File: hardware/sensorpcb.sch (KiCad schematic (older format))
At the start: 7 parts, among them P1 CONN_01X02

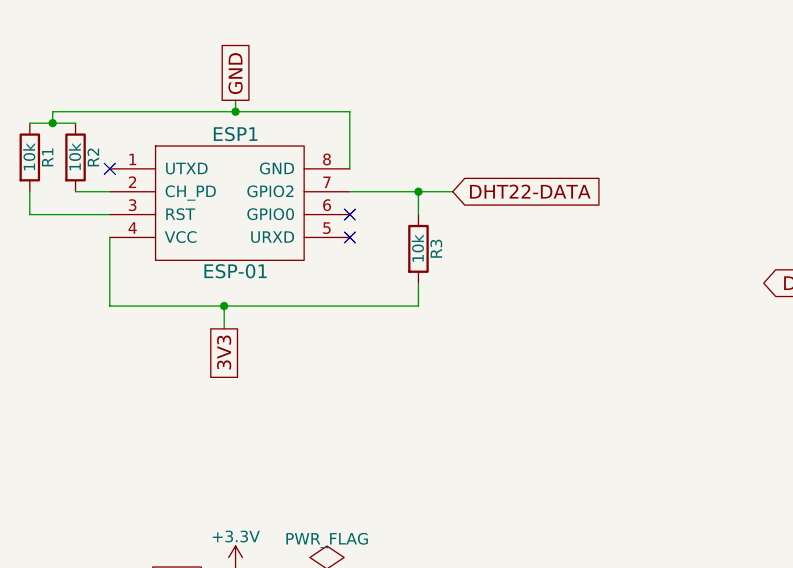
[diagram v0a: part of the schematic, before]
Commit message: corrected schematic: R1 and R2 are pullups, not pulldowns!
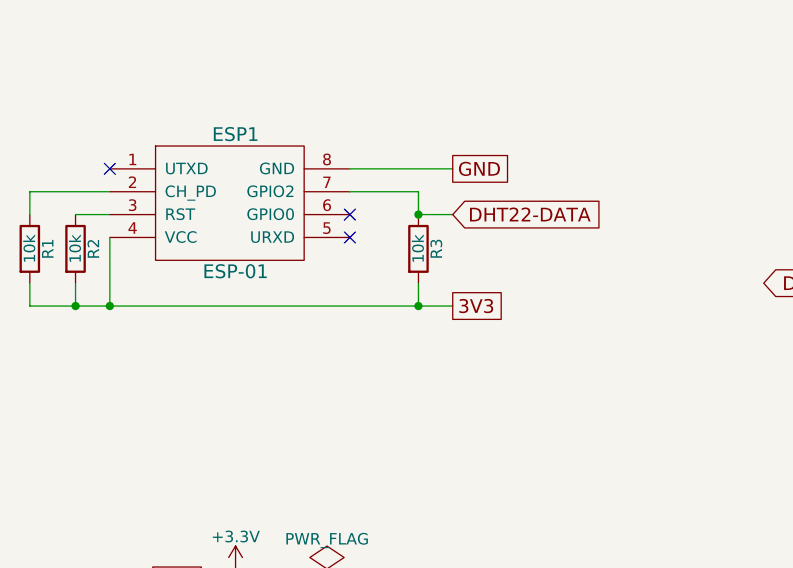
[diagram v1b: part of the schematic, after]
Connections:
- net +3V3: now also R1.2, R2.2
- net GNDREF: no longer R1.1, R2.1
- net at ESP1.2 (CH_PD): now also R1.1; no longer R2.2
- net at ESP1.3 (RST): now also R2.1; no longer R1.2
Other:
- moved on the sheet: R1, R2
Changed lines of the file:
@@
 LIBS:ESP8266
 LIBS:dht22
+LIBS:sensorpcb-cache
 EELAYER 25 0
 EELAYER END
@@
 Text GLabel 2000 3700 0    60   UnSpc ~ 0
 GND
-Text GLabel 3100 1600 2    60   Input ~ 0
+Text GLabel 3100 1700 2    60   Input ~ 0
 DHT22-DATA
 Text GLabel 5100 2000 0    60   Output ~ 0
@@
 Wire Wire Line
 	5050 1850 4950 1850
-Text GLabel 2150 1200 1    60   UnSpc ~ 0
+Text GLabel 3100 1500 2    60   UnSpc ~ 0
 GND
-Text GLabel 2100 2200 3    60   UnSpc ~ 0
+Text GLabel 3100 2100 2    60   UnSpc ~ 0
 3V3
 Wire Wire Line
 	1600 1800 1600 2100
-Wire Wire Line
-	2650 1250 2650 1500
 $Comp
 L CP C1
@@
 L R R1
 U 1 1 55FFEFC8
-P 1250 1450
-F 0 "R1" V 1330 1450 50  0000 C CNN
-F 1 "10k" V 1250 1450 50  0000 C CNN
-F 2 "" V 1180 1450 30  0000 C CNN
-F 3 "" H 1250 1450 30  0000 C CNN
-	1    1250 1450
+P 1250 1850
+F 0 "R1" V 1330 1850 50  0000 C CNN
+F 1 "10k" V 1250 1850 50  0000 C CNN
+F 2 "" V 1180 1850 30  0000 C CNN
+F 3 "" H 1250 1850 30  0000 C CNN
+	1    1250 1850
 	1    0    0    -1
 $EndComp
@@
 L R R2
 U 1 1 55FFF00F
-P 1450 1450
-F 0 "R2" V 1530 1450 50  0000 C CNN
-F 1 "10k" V 1450 1450 50  0000 C CNN
-F 2 "" V 1380 1450 30  0000 C CNN
-F 3 "" H 1450 1450 30  0000 C CNN
-	1    1450 1450
+P 1450 1850
+F 0 "R2" V 1530 1850 50  0000 C CNN
+F 1 "10k" V 1450 1850 50  0000 C CNN
+F 2 "" V 1380 1850 30  0000 C CNN
+F 3 "" H 1450 1850 30  0000 C CNN
+	1    1450 1850
 	1    0    0    -1
 $EndComp
@@
 $EndComp
 Wire Wire Line
-	1600 2100 2950 2100
-Wire Wire Line
-	2100 2100 2100 2200
-Connection ~ 2100 2100
-Wire Wire Line
-	2650 1600 3100 1600
+	1250 2100 3100 2100
 Wire Wire Line
 	2950 1700 2950 1600
-Connection ~ 2950 1600
 Wire Wire Line
 	5100 2000 5150 2000
 Wire Wire Line
 	5150 2000 5150 1850
-Wire Wire Line
-	1450 1600 1600 1600
-Wire Wire Line
-	1600 1700 1250 1700
-Wire Wire Line
-	1250 1700 1250 1600
-Wire Wire Line
-	1250 1300 1450 1300
-Wire Wire Line
-	1350 1300 1350 1250
-Wire Wire Line
-	1350 1250 2650 1250
-Wire Wire Line
-	2150 1250 2150 1200
-Connection ~ 1350 1300
-Connection ~ 2150 1250
 Wire Wire Line
 	2950 2100 2950 2000
@@
 Connection ~ 2550 3300
 Connection ~ 2550 3700
+Wire Wire Line
+	1250 1700 1250 1600
+Wire Wire Line
+	1250 1600 1600 1600
+Wire Wire Line
+	1450 1700 1600 1700
+Wire Wire Line
+	1250 2000 1250 2100
+Connection ~ 1600 2100
+Wire Wire Line
+	1450 2000 1450 2100
+Connection ~ 1450 2100
+Connection ~ 2950 2100
+Wire Wire Line
+	2950 1600 2650 1600
+Wire Wire Line
+	2950 1700 3100 1700
+Connection ~ 2950 1700
+Wire Wire Line
+	2650 1500 3100 1500
 $EndSCHEMATC

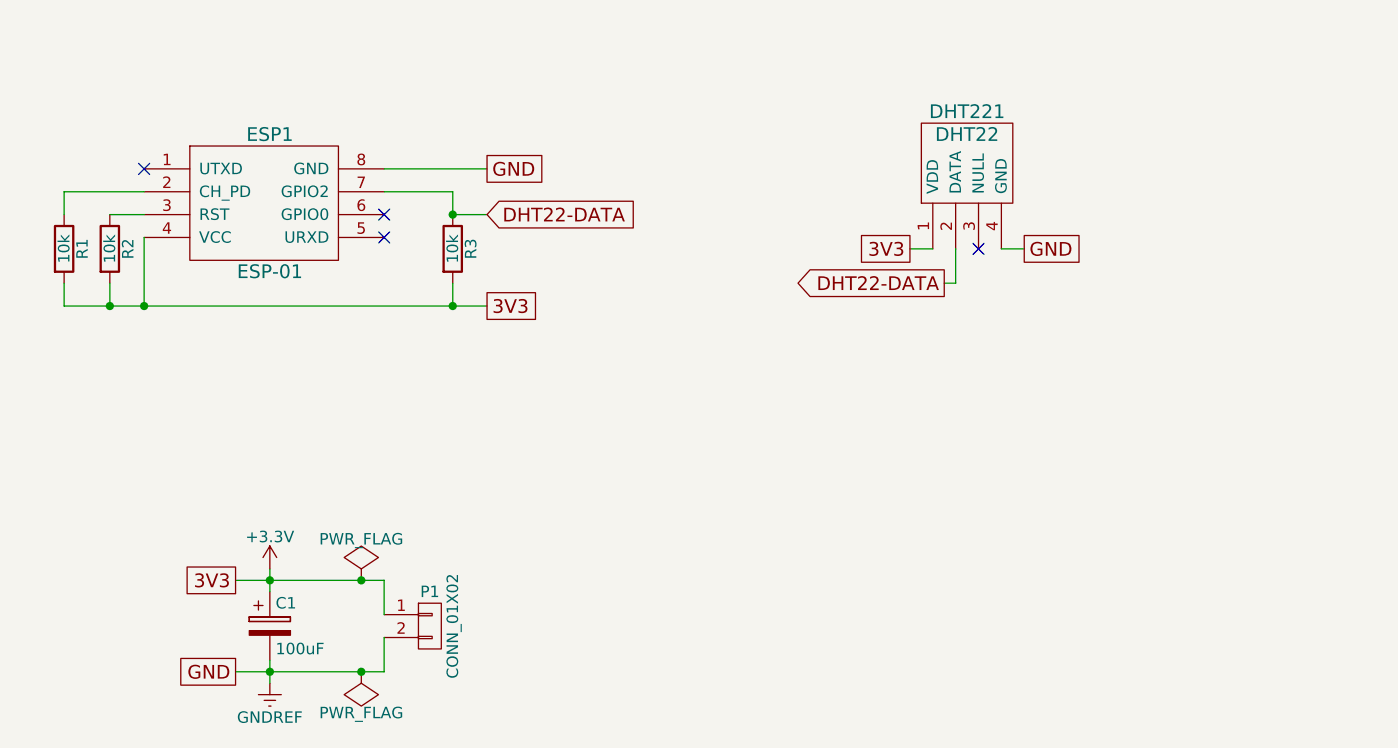
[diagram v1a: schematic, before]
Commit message: added DS18S20 to the schematic
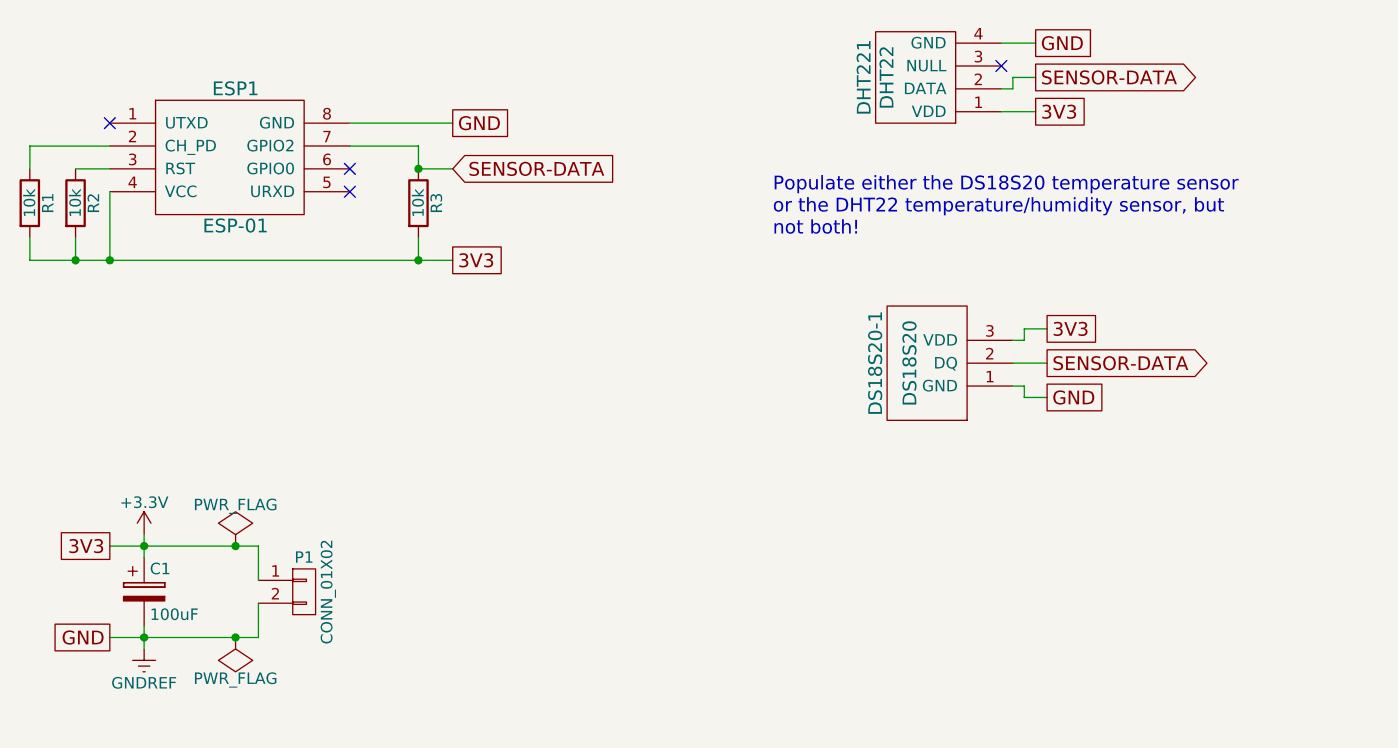
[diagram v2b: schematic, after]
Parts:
- added DS18S20-1: DS18S20, symbol DS18S20
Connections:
- net +3V3: now also DS18S20-1.3 (VDD)
- net GNDREF: now also DS18S20-1.1 (GND)
- net DHT22-DATA renamed SENSOR-DATA
- net SENSOR-DATA: now also DS18S20-1.2 (DQ)
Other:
- note added: "Populate either the DS18S20 temperature sensor\nor the DHT22 temperature/humidity sensor, but \nnot both!"
- moved on the sheet: C1, DHT221, ESP1, P1, R1, R2, R3
